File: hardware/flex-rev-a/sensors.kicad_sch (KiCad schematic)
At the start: 0 parts

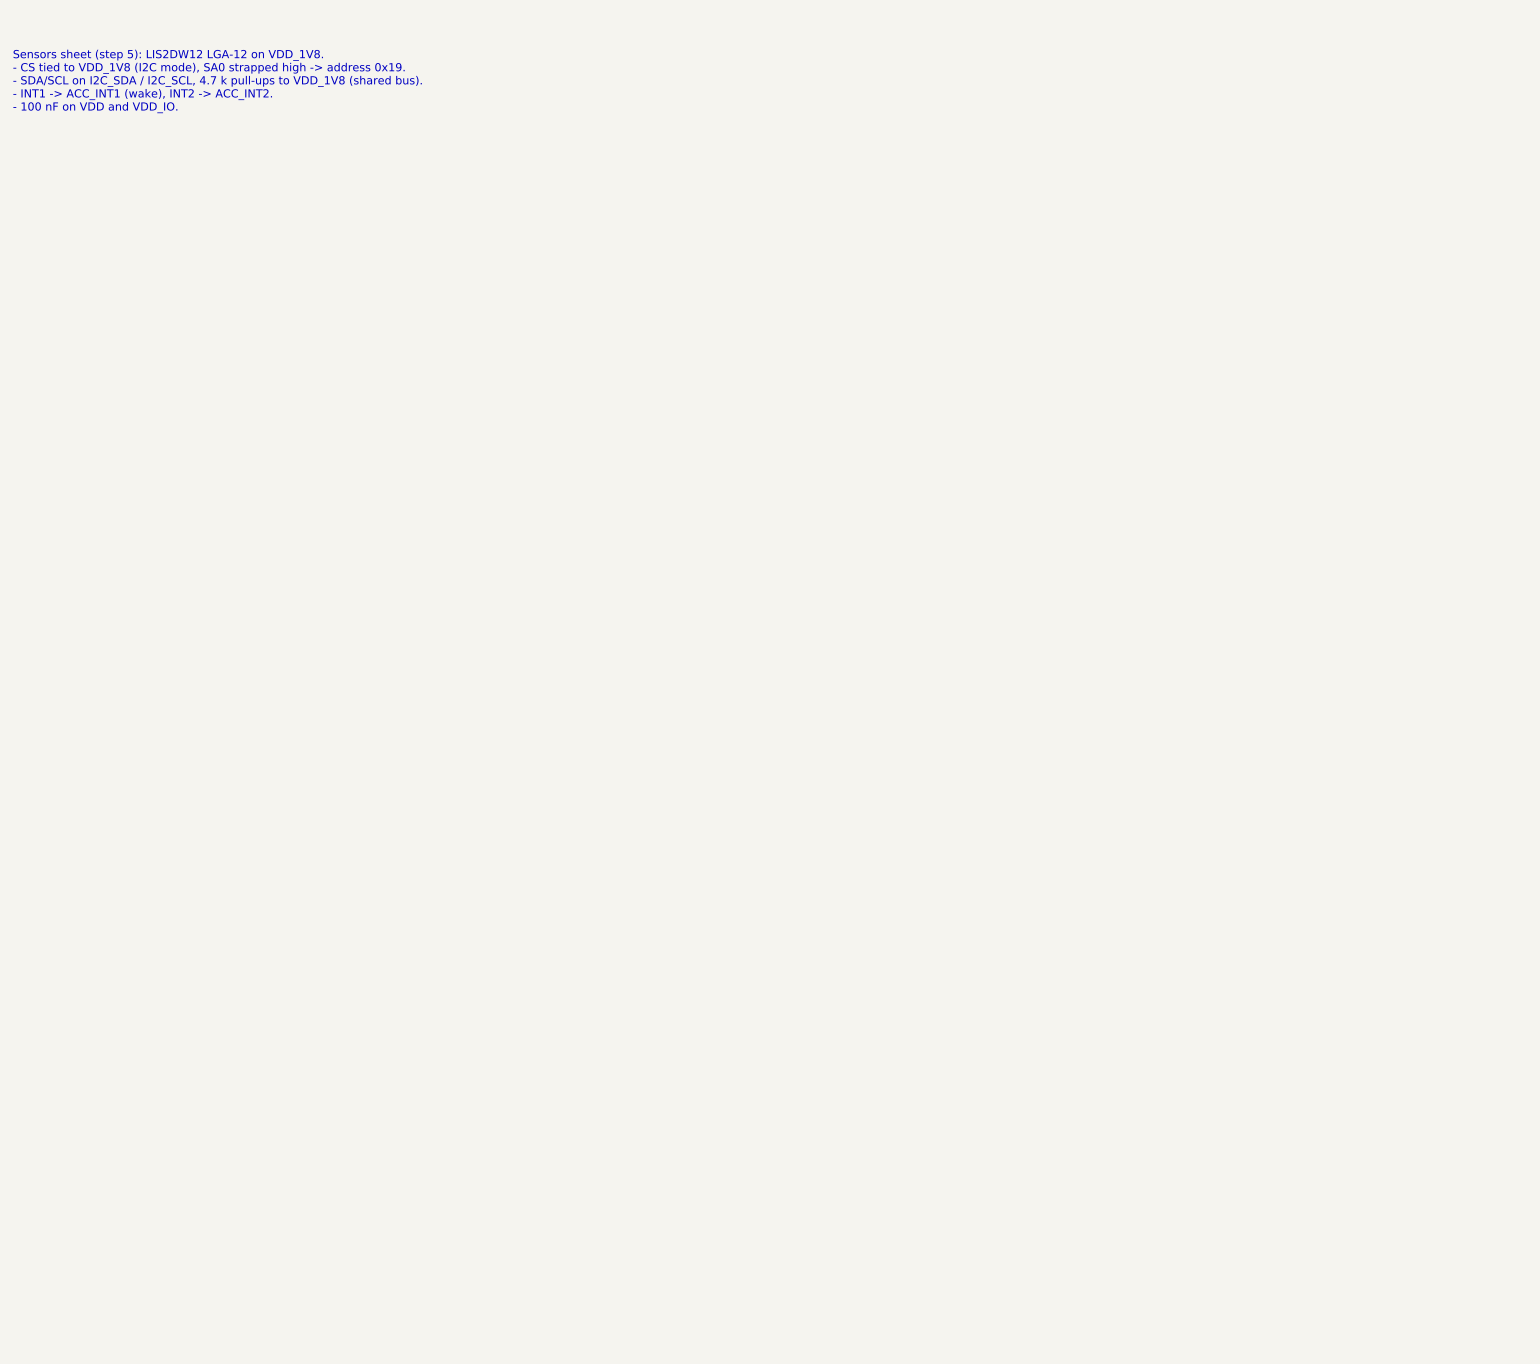
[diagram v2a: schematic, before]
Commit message: Draw sensors sheet: LIS2DW12 accelerometer on the 1.8 V I2C bus
From ST datasheet DocID029682 Rev 4, table 2:
- VDD (9) and VDD_IO (10) on VDD_1V8, 100 nF on each.
- CS (2) and SDO/SA0 (3) tied to VDD_1V8: I2C mode, address 0x19.
- SDA/SCL on I2C_SDA/I2C_SCL (pull-ups stay on the power sheet).
- INT1 -> ACC_INT1, INT2 -> ACC_INT2 with test pad TP401.
- NC (5) and RES (7) to GND as the datasheet allows/requires.
- New LIS2DW12 project symbol; KiCad LGA-12 2x2 footprint (check vs ST).
- Project footprints added: 0.8 mm test pad, LRA lead pad, 6-pad dock
  strip; library saved in KiCad 10 format.

ERC: 2 errors, 9 warnings, none on the power or sensors sheets.

Co-Authored-By: Claude Opus 5.5 <noreply@anthropic.com>
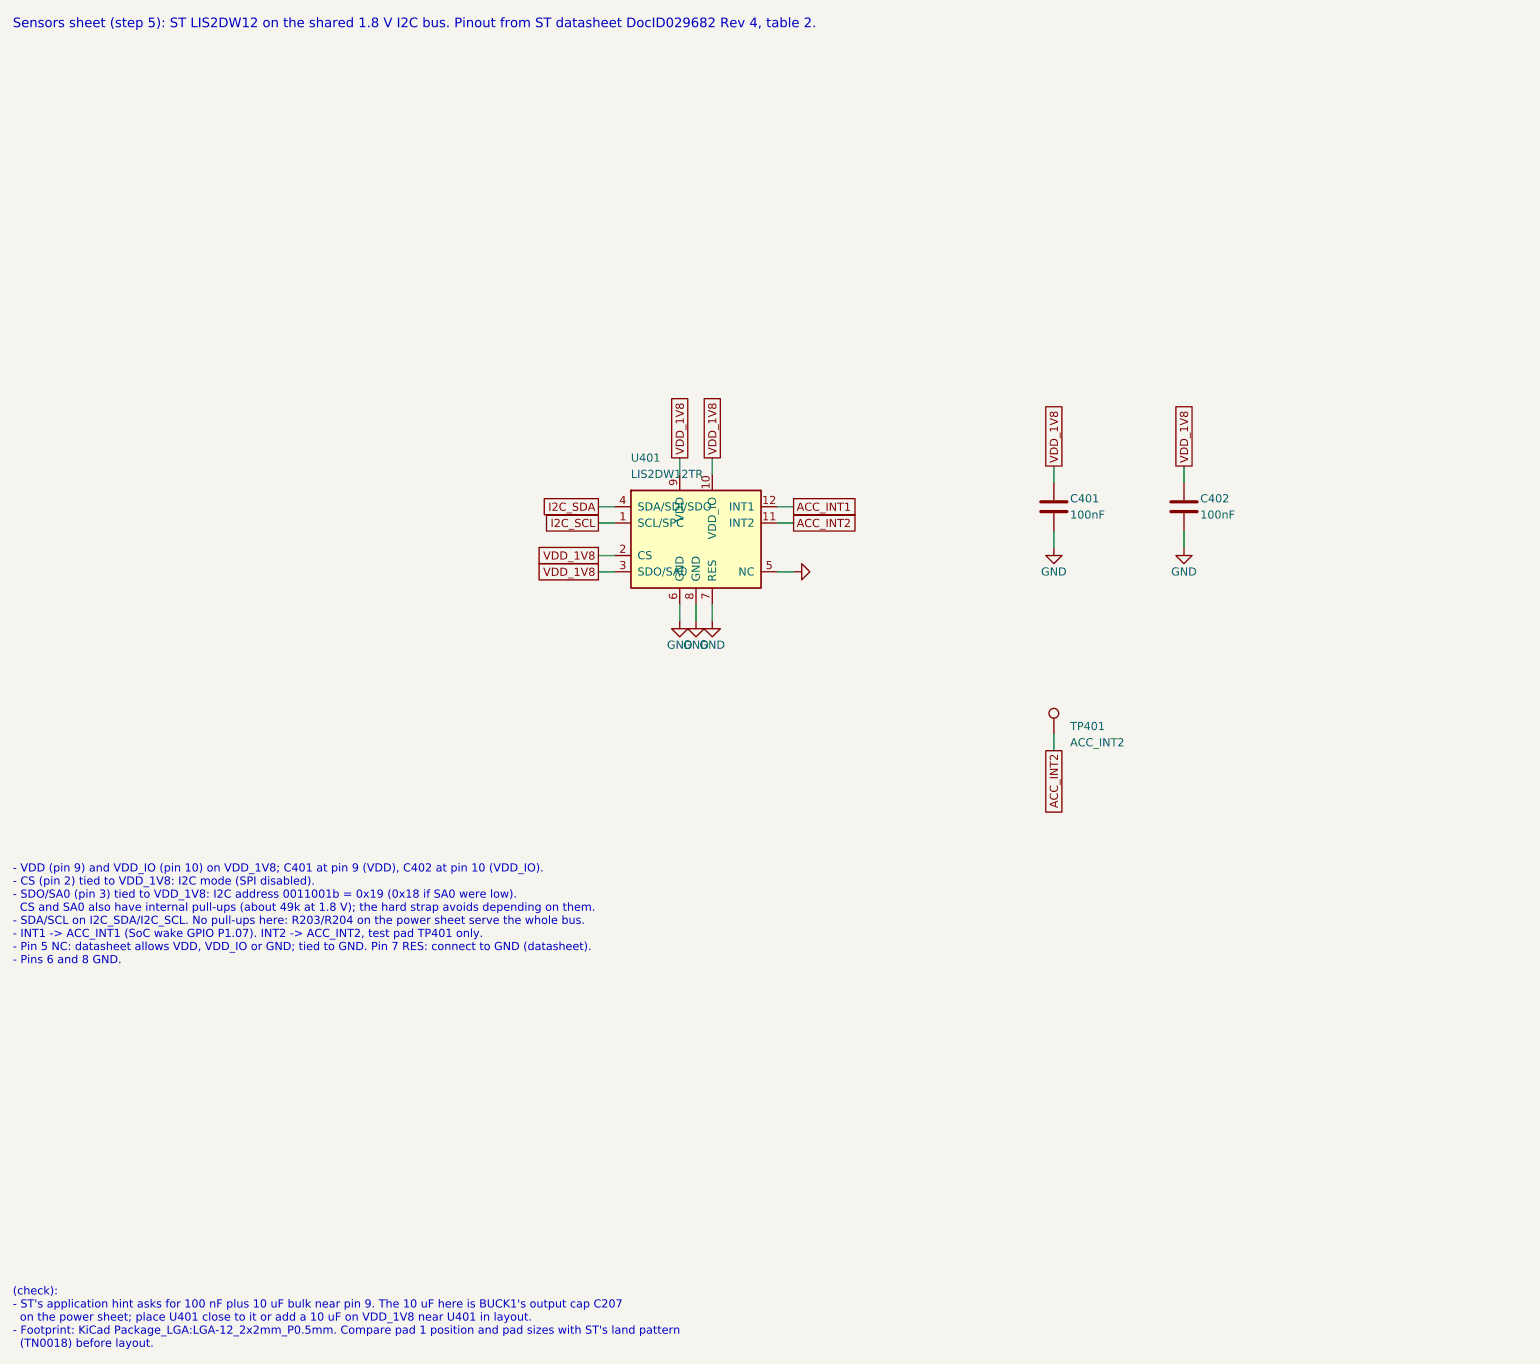
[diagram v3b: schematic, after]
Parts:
- added C401, C402: 100nF, Capacitor_SMD:C_0402_1005Metric, symbol Device:C
- added TP401: ACC_INT2, wakeband:TestPoint_Pad_D0.8mm, symbol Connector:TestPoint
- added U401: LIS2DW12TR, Package_LGA:LGA-12_2x2mm_P0.5mm, symbol wakeband:LIS2DW12
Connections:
- new net ACC_INT1: U401.12 (INT1)
- new net ACC_INT2: TP401.1, U401.11 (INT2)
- new net GND: C401.2, C402.2, U401.5 (NC), U401.6 (GND), U401.7 (RES), U401.8 (GND)
- new net I2C_SCL: U401.1 (SCL/SPC)
- new net I2C_SDA: U401.4 (SDA/SDI/SDO)
- new net VDD_1V8: C401.1, C402.1, U401.10 (VDD_IO), U401.2 (CS), U401.3 (SDO/SA0), U401.9 (VDD)
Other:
- note added: "(check): - ST's application hint asks for 100 nF plus 10 uF bulk near pin 9. The 10 uF here is BUCK1's output cap C207 on the power sheet; place U401 close to it or add a 10 uF on VDD_1V8 near U401 in layout. - Footprint: KiCad Package_LGA:LGA-12_2x2mm_P0.5mm. Compare pad 1 position and pad sizes with ST's land pattern (TN0018) before layout."
- note added: "- VDD (pin 9) and VDD_IO (pin 10) on VDD_1V8; C401 at pin 9 (VDD), C402 at pin 10 (VDD_IO). - CS (pin 2) tied to VDD_1V8: I2C mode (SPI disabled). - SDO/SA0 (pin 3) tied to VDD_1V8: I2C address 0011001b = 0x19 (0x18 if SA0 were low). CS and SA0 also have internal pull-ups (about 49k at 1.8 V); the hard strap avoids depending on them. - SDA/SCL on I2C_SDA/I2C_SCL. No pull-ups here: R203/R204 on th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"
- note added: "Sensors sheet (step 5): ST LIS2DW12 on the shared 1.8 V I2C bus. Pinout from ST datasheet DocID029682 Rev 4, table 2."
- note removed: "Sensors sheet (step 5): LIS2DW12 LGA-12 on VDD_1V8. - CS tied to VDD_1V8 (I2C mode), SA0 strapped high -> address 0x19. - SDA/SCL on I2C_SDA / I2C_SCL, 4.7 k pull-ups to VDD_1V8 (shared bus). - INT1 -> ACC_INT1 (wake), INT2 -> ACC_INT2. - 100 nF on VDD and VDD_IO."

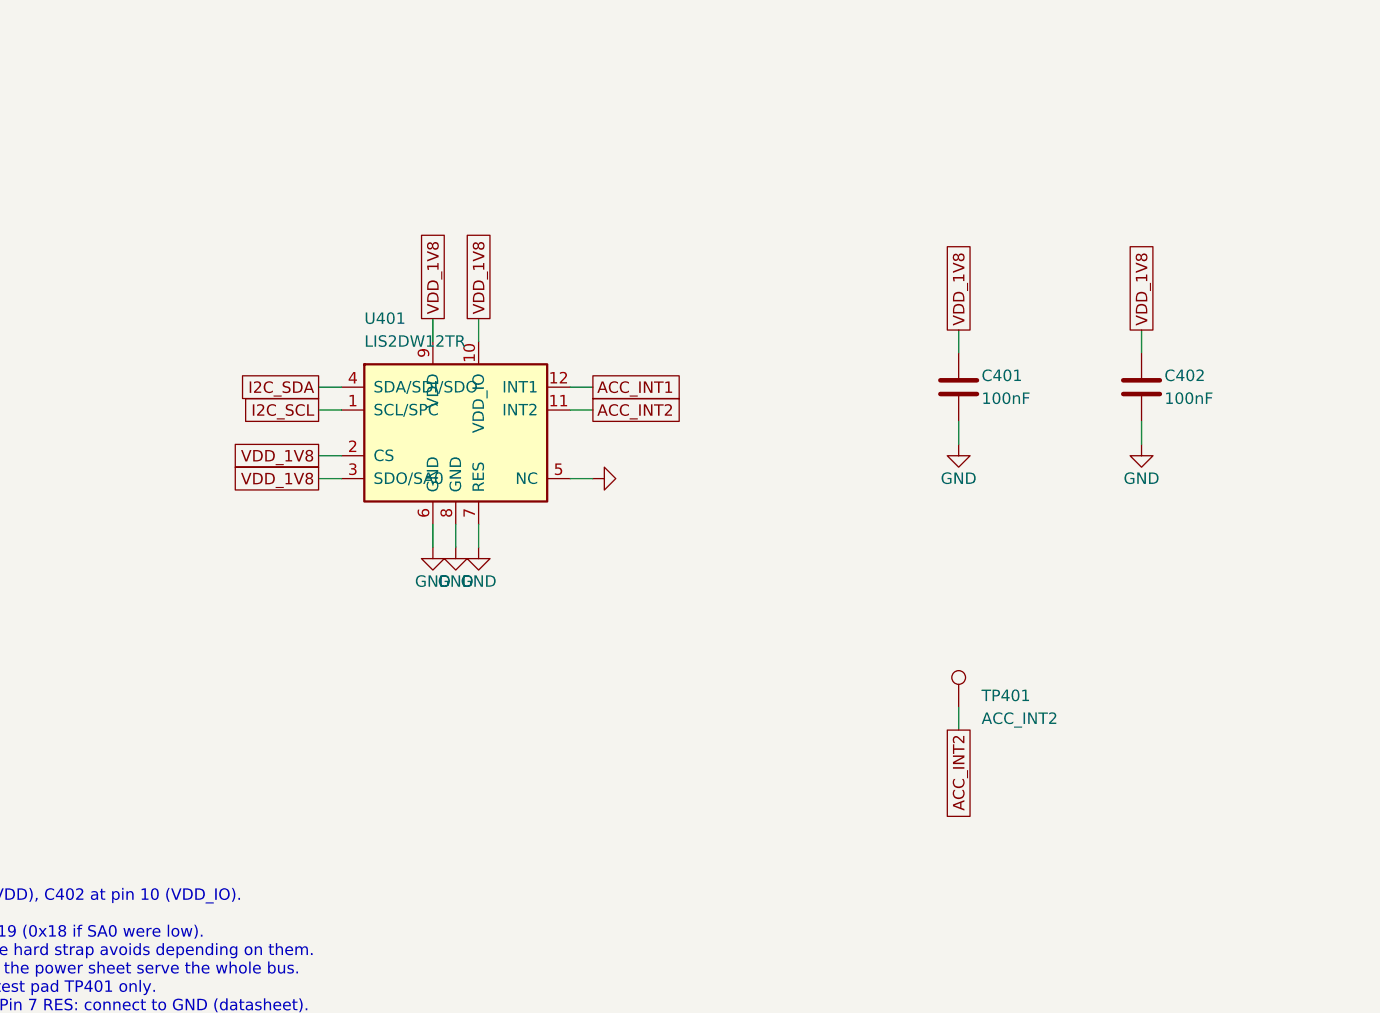
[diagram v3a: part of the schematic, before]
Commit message: Finish rev A schematic pass: clean ERC, BOM with LCSC numbers
- ERC 0 errors, 0 warnings: the ISP2454 symbol's ground pins renamed from
  VSS to GND (same pins), so they no longer clash with the GND label.
- Sensors: larger LIS2DW12 symbol so pin names and GND symbols no longer
  overlap. Dock: connector mirrored and TVS spacing widened for
  readability. No connectivity changes.
- bom.csv: JLCPCB-style columns with LCSC numbers checked on lcsc.com;
  ISP2454-LX and nPM1304-QEAA have none. Pads, jumper and net tie excluded.
- All 50 references annotated and unique; PDF replotted; README status
  table, ERC notes and plan progress updated.

Co-Authored-By: Claude Opus 5.5 <noreply@anthropic.com>
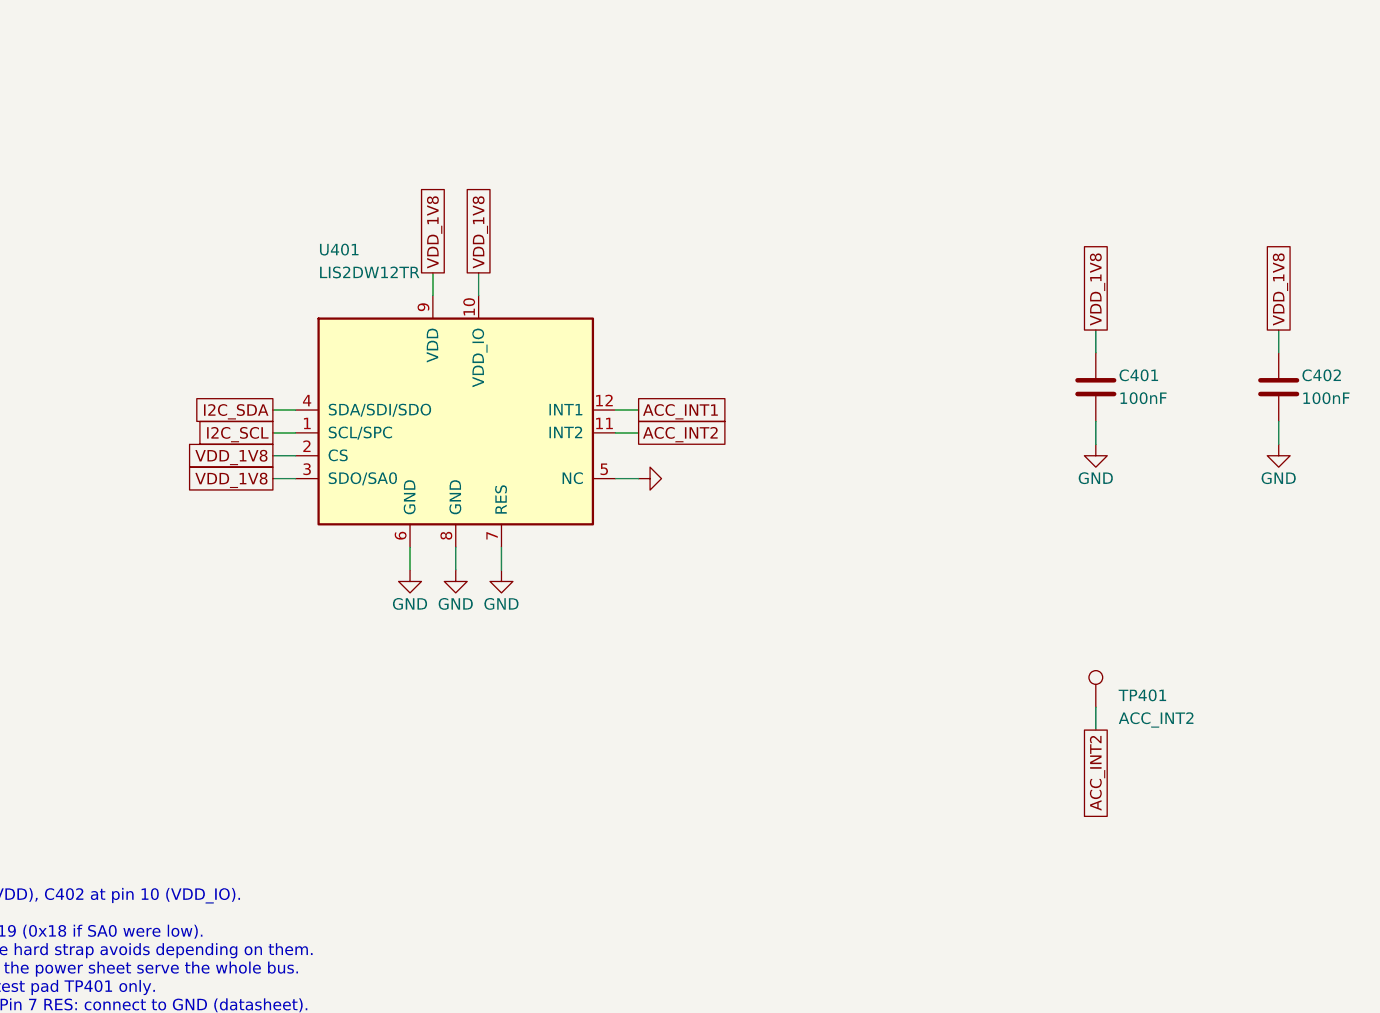
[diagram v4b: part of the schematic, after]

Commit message: Apply schematic review fixes: 2.0 V rail, pad 10 NC, VIN TVS, bulk cap
- Power: R202 47k -> 68k so BUCK1 starts at 2.0 V; global net VDD_1V8
  renamed VDD_2V0 on every sheet, notes updated.
- Haptics: DRV2605L IN/TRIG tied to GND, HAPT_TRIG removed (effects run
  over I2C). Footprint kept as Package_SO:TSSOP-10_3x3mm_P0.5mm: it is
  KiCad's TI DGS land pattern (cites MPDS035); KiCad 10 has no footprint
  named VSSOP-10_3x3mm_P0.5mm.
- MCU: pad 10 (P1.10) no-connect; GND global label replaced by the GND
  power symbol; note on the trapped lower-row GND pads 12/14/16/18 and on
  pads 8/24.
- Sensors: C403 10 uF on LIS2DW12 VDD per ST; related (check) removed.
- Dock: VIN TVS is now Littelfuse SMF18A (SOD-123FL, 18 V standoff, LCSC
  C409420); data pads keep TPD1E10B06, TPD1E0B04 noted as a lower-leakage
  alternative (check).
- bom.csv regenerated, PDF replotted, README updated.

ERC: 0 errors, 0 warnings.

Co-Authored-By: Claude Opus 5.5 <noreply@anthropic.com>
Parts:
- added C403: 10uF 25V X5R, Capacitor_SMD:C_0603_1608Metric, symbol Device:C
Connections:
- net GND: now also C403.2
- net VDD_1V8 renamed VDD_2V0
- net VDD_2V0: now also C403.1
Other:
- note added: "(check): - Footprint: KiCad Package_LGA:LGA-12_2x2mm_P0.5mm. Compare pad 1 position and pad sizes with ST's land pattern (TN0018) before layout."
- note added: "- VDD (pin 9) and VDD_IO (pin 10) on VDD_2V0; C401 at pin 9 (VDD), C402 at pin 10 (VDD_IO). - C403 10 uF bulk on VDD near pin 9, per ST's application hint (100 nF + 10 uF). - CS (pin 2) tied to VDD_2V0: I2C mode (SPI disabled). - SDO/SA0 (pin 3) tied to VDD_2V0: I2C address 0011001b = 0x19 (0x18 if SA0 were low). CS and SA0 also have internal pull-ups (about 49k at 1.8 V, 30k at 2.5 V); the hard 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"
- note added: "Sensors sheet (step 5): ST LIS2DW12 on the shared 2.0 V I2C bus. Pinout from ST datasheet DocID029682 Rev 4, table 2."
- note removed: "(check): - ST's application hint asks for 100 nF plus 10 uF bulk near pin 9. The 10 uF here is BUCK1's output cap C207 on the power sheet; place U401 close to it or add a 10 uF on VDD_1V8 near U401 in layout. - Footprint: KiCad Package_LGA:LGA-12_2x2mm_P0.5mm. Compare pad 1 position and pad sizes with ST's land pattern (TN0018) before layout."
- note removed: "- VDD (pin 9) and VDD_IO (pin 10) on VDD_1V8; C401 at pin 9 (VDD), C402 at pin 10 (VDD_IO). - CS (pin 2) tied to VDD_1V8: I2C mode (SPI disabled). - SDO/SA0 (pin 3) tied to VDD_1V8: I2C address 0011001b = 0x19 (0x18 if SA0 were low). CS and SA0 also have internal pull-ups (about 49k at 1.8 V); the hard strap avoids depending on them. - SDA/SCL on I2C_SDA/I2C_SCL. No pull-ups here: R203/R204 on th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"
- note removed: "Sensors sheet (step 5): ST LIS2DW12 on the shared 1.8 V I2C bus. Pinout from ST datasheet DocID029682 Rev 4, table 2."
